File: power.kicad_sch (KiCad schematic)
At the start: 85 parts, among them Q10 2NPN, Q3 PMOS, Q4 PMOS, Q5 PMOS, Q6 PMOS, Q7 2NPN, Q9 2PNP, U21 TPS62410, U22 LDO-2V5, U28 AP22652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

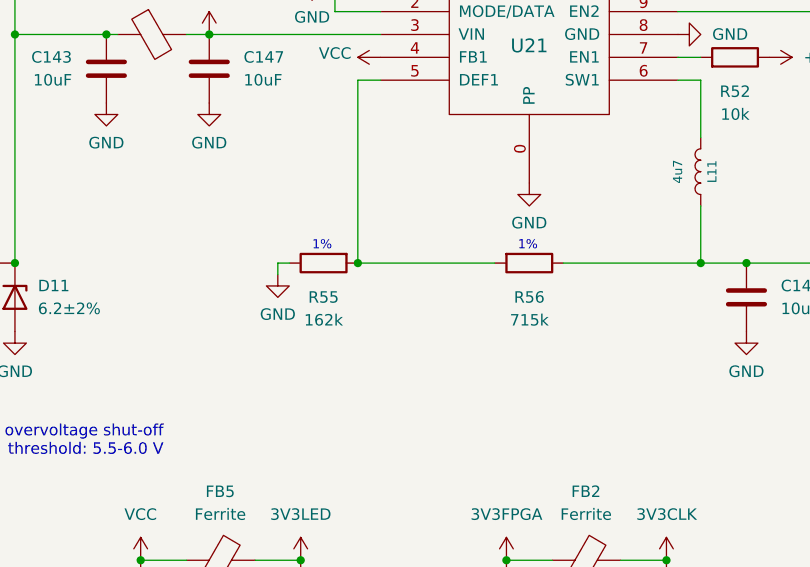
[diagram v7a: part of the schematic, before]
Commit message: Increase VCC from 3.25 V to 3.33 V
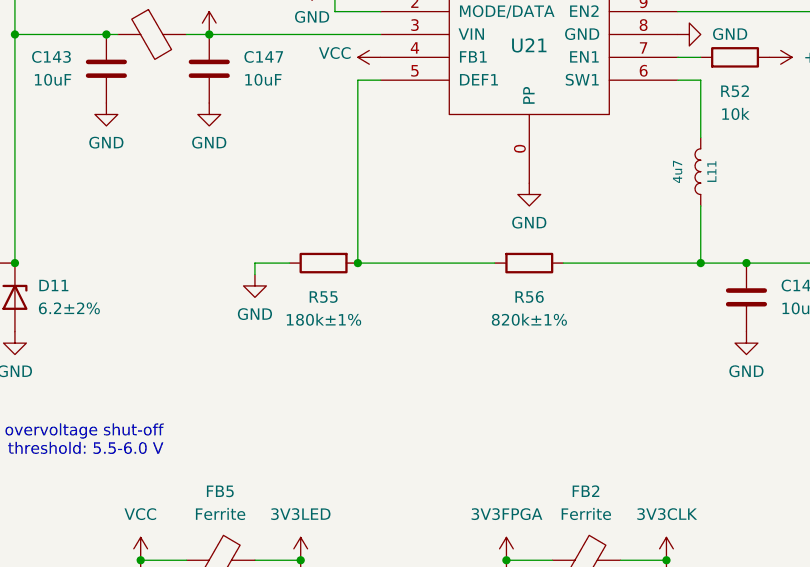
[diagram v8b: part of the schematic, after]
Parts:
- R55: value 162k -> 180k±1%; Part Number RC0402FR-07162KL -> RC0402FR-07180KL
- R56: value 715k -> 820k±1%; Part Number RC0402FR-07715KL -> RC0402FR-07820KL
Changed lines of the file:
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@@
 	(wire
 		(pts
-			(xy 120.65 76.2) (xy 121.92 76.2)
+			(xy 118.11 76.2) (xy 121.92 76.2)
 		)
 		(stroke
@@
 	(wire
 		(pts
-			(xy 120.65 77.47) (xy 120.65 76.2)
+			(xy 118.11 77.47) (xy 118.11 76.2)
 		)
 		(stroke
@@
 		)
 	)
-	(text "1%"
-		(exclude_from_sim no)
-		(at 124.46 74.93 0)
-		(effects
-			(font
-				(size 1.016 1.016)
-			)
-			(justify left bottom)
-		)
-	)
-	(text "1%"
-		(exclude_from_sim no)
-		(at 147.32 74.93 0)
-		(effects
-			(font
-				(size 1.016 1.016)
-			)
-			(justify left bottom)
-		)
-	)
 	(label "VBUS"
 		(at 46.99 185.42 90)
@@
 	(symbol
 		(lib_id "power:GND")
-		(at 120.65 77.47 0)
+		(at 118.11 77.47 0)
 		(unit 1)
 		(exclude_from_sim no)
@@
 		(fields_autoplaced yes)
 		(property "Reference" "#PWR0171"
-			(at 120.65 83.82 0)
+			(at 118.11 83.82 0)
 			(effects
 				(font
@@
 		)
 		(property "Value" "GND"
-			(at 120.65 81.9134 0)
+			(at 118.11 81.9134 0)
 			(effects
 				(font
@@
 		)
 		(property "Footprint" ""
-			(at 120.65 77.47 0)
+			(at 118.11 77.47 0)
 			(effects
 				(font
@@
 		)
 		(property "Datasheet" ""
-			(at 120.65 77.47 0)
+			(at 118.11 77.47 0)
 			(effects
 				(font
@@
 		)
 		(property "Description" "Power symbol creates a global label with name \"GND\" , ground"
-			(at 120.65 77.47 0)
+			(at 118.11 77.47 0)
 			(effects
 				(font
@@
 			)
 		)
-		(property "Value" "162k"
+		(property "Value" "180k±1%"
 			(at 125.73 82.55 90)
 			(effects
@@
 			)
 		)
-		(property "Description" "RES 1/16W 162K OHM 1% 0402"
+		(property "Description" "RES 180K OHM 1% 1/16W 0402"
 			(at 125.73 76.2 0)
 			(effects
@@
 			)
 		)
-		(property "Part Number" "RC0402FR-07162KL"
+		(property "Part Number" "RC0402FR-07180KL"
 			(at 125.73 76.2 0)
 			(effects
@@
 			)
 		)
-		(property "Value" "715k"
+		(property "Value" "820k±1%"
 			(at 148.59 82.55 90)
 			(effects
@@
 			)
 		)
-		(property "Description" "RES 1/16W 715K OHM 1% 0402"
+		(property "Description" "RES 820K OHM 1% 1/16W 0402"
 			(at 148.59 76.2 0)
 			(effects
@@
 			)
 		)
-		(property "Part Number" "RC0402FR-07715KL"
+		(property "Part Number" "RC0402FR-07820KL"
 			(at 148.59 76.2 0)
 			(effects
